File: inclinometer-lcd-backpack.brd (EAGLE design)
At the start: 78.7 x 25.4 mm, 15 parts, among them IC1 ATmega328-DIP-Prgrammed, Q1 2N3904, U1 LCD-16X2NOHOLES, Y1 16MHz

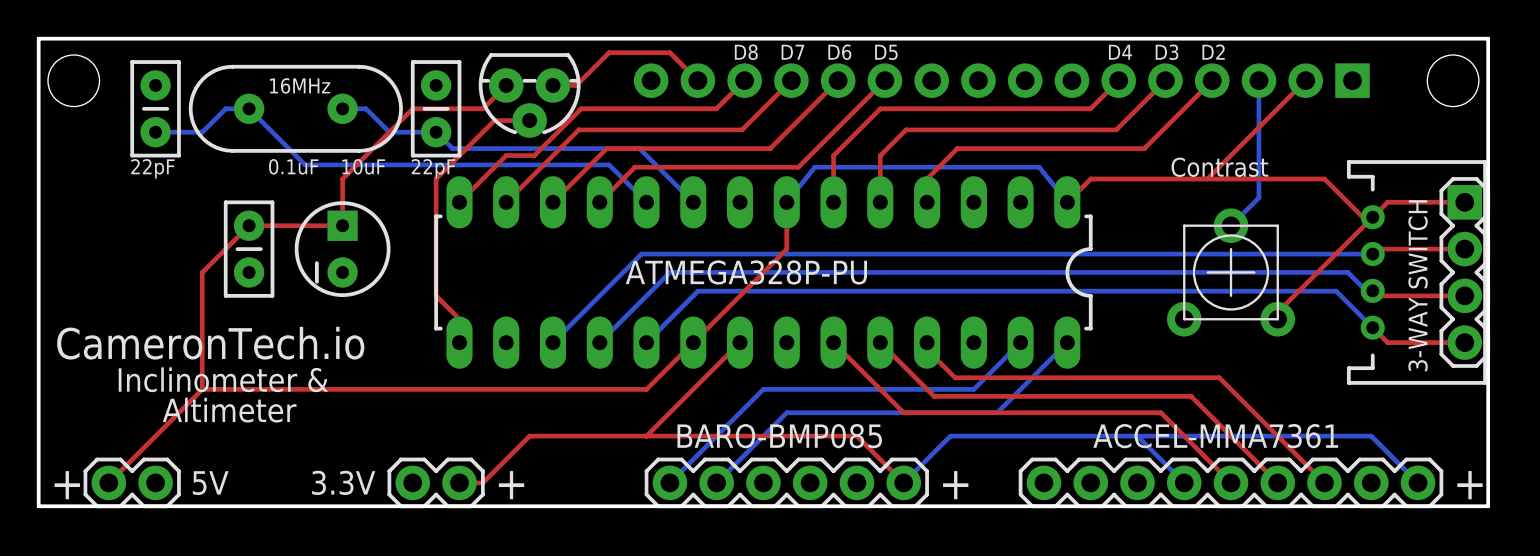
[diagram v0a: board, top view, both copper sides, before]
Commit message: Moved pins away from bottom edge, updated silkscreen
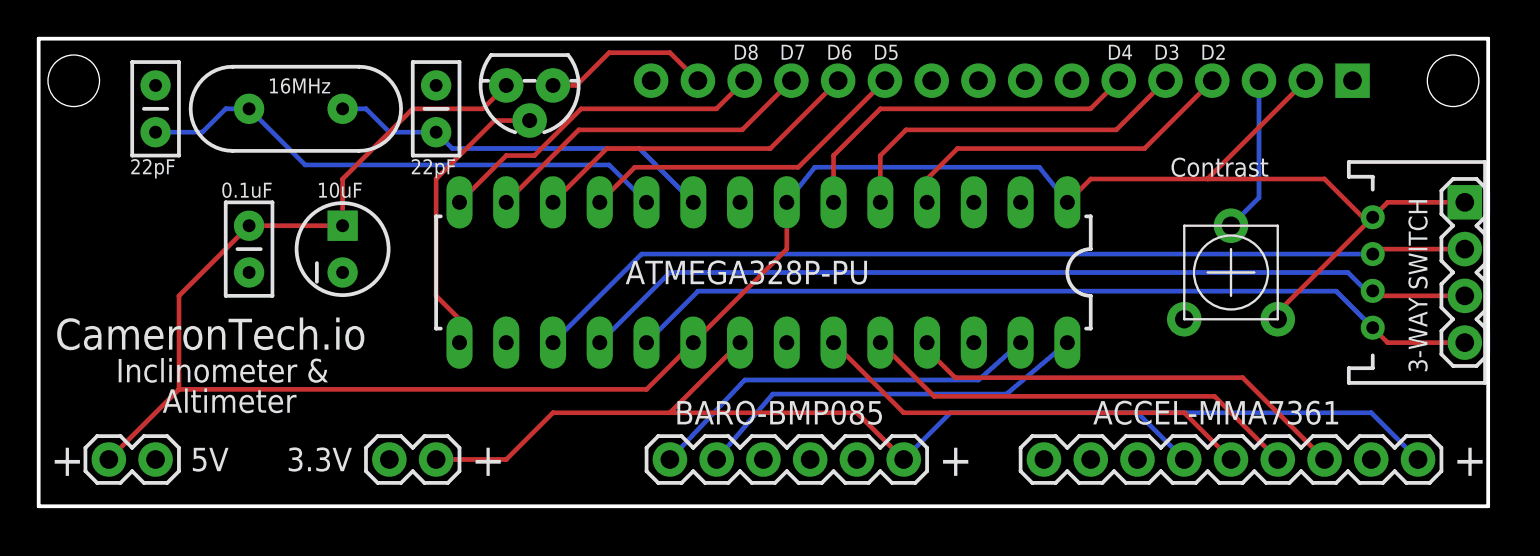
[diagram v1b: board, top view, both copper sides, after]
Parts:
- moved 3.3V 1.80 mm to (19.1, 2.54)
- moved 5V 1.27 mm to (6.35, 2.54)
- moved ACCEL 1.27 mm to (54.6, 2.54)
- moved BARO 1.27 mm to (47.0, 2.54)
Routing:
- net A2: track 25.0 -> 24.4 mm
- net A1: track 24.7 -> 24.2 mm
- net A0: track 24.7 -> 24.2 mm
- net 3.3V: track 67.1 -> 66.5 mm
- net A4: track 22.2 -> 21.7 mm

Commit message: Changes 3-way switch from 5V to GND, beefs up power connections to 0.016 wire width
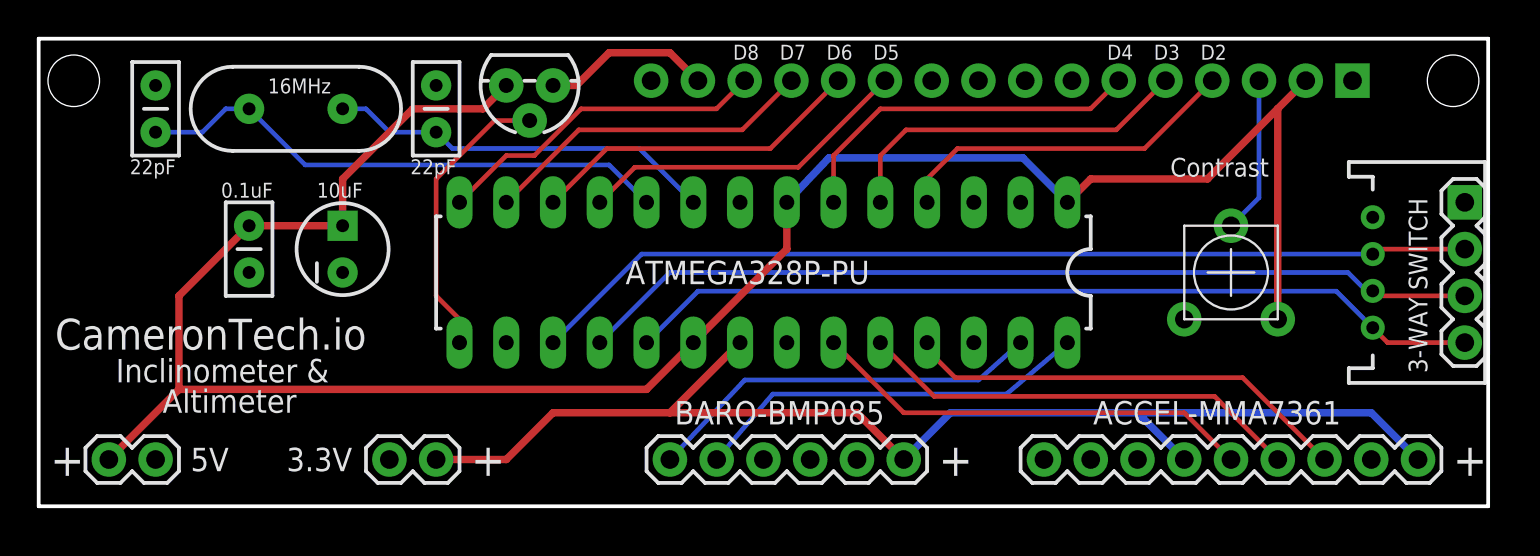
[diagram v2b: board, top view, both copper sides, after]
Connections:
- net 5V: no longer SWITCH-JST.1, SWITCH.1
- net GND: now also SWITCH-JST.1, SWITCH.1
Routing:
- net 5V: track 128.8 -> 117.6 mm
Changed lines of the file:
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@@
 <grid distance="0.05" unitdist="inch" unit="inch" style="lines" multiple="1" display="yes" altdistance="0.005" altunitdist="inch" altunit="inch"/>
 <layers>
-<layer number="1" name="Top" color="4" fill="1" visible="no" active="yes"/>
+<layer number="1" name="Top" color="4" fill="1" visible="yes" active="yes"/>
 <layer number="2" name="Route2" color="1" fill="3" visible="no" active="no"/>
 <layer number="3" name="Route3" color="4" fill="3" visible="no" active="no"/>
@@
 <layer number="14" name="Route14" color="1" fill="6" visible="no" active="no"/>
 <layer number="15" name="Route15" color="4" fill="6" visible="no" active="no"/>
-<layer number="16" name="Bottom" color="1" fill="1" visible="no" active="yes"/>
+<layer number="16" name="Bottom" color="1" fill="1" visible="yes" active="yes"/>
 <layer number="17" name="Pads" color="2" fill="1" visible="yes" active="yes"/>
 <layer number="18" name="Vias" color="2" fill="1" visible="yes" active="yes"/>
@@
 <layer number="21" name="tPlace" color="16" fill="1" visible="no" active="yes"/>
 <layer number="22" name="bPlace" color="14" fill="1" visible="yes" active="yes"/>
-<layer number="23" name="tOrigins" color="15" fill="1" visible="no" active="yes"/>
-<layer number="24" name="bOrigins" color="15" fill="1" visible="no" active="yes"/>
+<layer number="23" name="tOrigins" color="15" fill="1" visible="yes" active="yes"/>
+<layer number="24" name="bOrigins" color="15" fill="1" visible="yes" active="yes"/>
 <layer number="25" name="tNames" color="7" fill="1" visible="no" active="yes"/>
-<layer number="26" name="bNames" color="7" fill="1" visible="yes" active="yes"/>
+<layer number="26" name="bNames" color="7" fill="1" visible="no" active="yes"/>
 <layer number="27" name="tValues" color="7" fill="1" visible="no" active="yes"/>
 <layer number="28" name="bValues" color="7" fill="1" visible="no" active="yes"/>
@@
 <layer number="49" name="Reference" color="7" fill="1" visible="no" active="yes"/>
 <layer number="50" name="dxf" color="7" fill="1" visible="no" active="yes"/>
-<layer number="51" name="tDocu" color="6" fill="1" visible="no" active="yes"/>
+<layer number="51" name="tDocu" color="6" fill="1" visible="yes" active="yes"/>
 <layer number="52" name="bDocu" color="7" fill="1" visible="no" active="yes"/>
 <layer number="53" name="tGND_GNDA" color="7" fill="9" visible="no" active="no"/>
@@
 <contactref element="U1" pad="2"/>
 <contactref element="Q1" pad="3"/>
-<wire x1="24.13" y1="21.59" x2="25.4" y2="22.86" width="0.254" layer="1"/>
-<wire x1="20.32" y1="21.59" x2="24.13" y2="21.59" width="0.254" layer="1"/>
-<wire x1="11.43" y1="15.24" x2="16.51" y2="15.24" width="0.254" layer="1"/>
-<wire x1="16.51" y1="15.24" x2="16.51" y2="17.78" width="0.254" layer="1"/>
-<wire x1="16.51" y1="17.78" x2="20.32" y2="21.59" width="0.254" layer="1"/>
-<wire x1="33.02" y1="6.35" x2="35.56" y2="8.89" width="0.254" layer="1"/>
-<wire x1="40.64" y1="13.97" x2="40.64" y2="16.51" width="0.254" layer="1"/>
-<wire x1="7.62" y1="11.43" x2="11.43" y2="15.24" width="0.254" layer="1"/>
-<wire x1="7.62" y1="11.43" x2="7.62" y2="6.35" width="0.254" layer="1"/>
+<wire x1="24.13" y1="21.59" x2="25.4" y2="22.86" width="0.4064" layer="1"/>
+<wire x1="20.32" y1="21.59" x2="24.13" y2="21.59" width="0.4064" layer="1"/>
+<wire x1="11.43" y1="15.24" x2="16.51" y2="15.24" width="0.4064" layer="1"/>
+<wire x1="16.51" y1="15.24" x2="16.51" y2="17.78" width="0.4064" layer="1"/>
+<wire x1="16.51" y1="17.78" x2="20.32" y2="21.59" width="0.4064" layer="1"/>
+<wire x1="33.02" y1="6.35" x2="35.56" y2="8.89" width="0.4064" layer="1"/>
+<wire x1="40.64" y1="13.97" x2="40.64" y2="16.51" width="0.4064" layer="1"/>
+<wire x1="7.62" y1="11.43" x2="11.43" y2="15.24" width="0.4064" layer="1"/>
+<wire x1="7.62" y1="11.43" x2="7.62" y2="6.35" width="0.4064" layer="1"/>
 <contactref element="5V" pad="2"/>
-<wire x1="3.81" y1="2.54" x2="7.62" y2="6.35" width="0.254" layer="1"/>
-<wire x1="33.02" y1="6.35" x2="7.62" y2="6.35" width="0.254" layer="1"/>
-<wire x1="35.56" y1="8.89" x2="40.64" y2="13.97" width="0.254" layer="1"/>
+<wire x1="3.81" y1="2.54" x2="7.62" y2="6.35" width="0.4064" layer="1"/>
+<wire x1="33.02" y1="6.35" x2="7.62" y2="6.35" width="0.4064" layer="1"/>
+<wire x1="35.56" y1="8.89" x2="40.64" y2="13.97" width="0.4064" layer="1"/>
 <contactref element="R2" pad="3"/>
-<contactref element="SWITCH-JST" pad="1"/>
 <contactref element="IC1" pad="1"/>
-<wire x1="55.88" y1="16.51" x2="57.15" y2="17.78" width="0.254" layer="1"/>
-<wire x1="57.15" y1="17.78" x2="63.5" y2="17.78" width="0.254" layer="1"/>
-<wire x1="63.5" y1="17.78" x2="69.85" y2="17.78" width="0.254" layer="1"/>
-<wire x1="69.85" y1="17.78" x2="71.93" y2="15.7" width="0.254" layer="1"/>
-<wire x1="71.93" y1="15.7" x2="72.47" y2="15.7" width="0.254" layer="1"/>
-<wire x1="68.83" y1="23.12" x2="63.5" y2="17.79" width="0.254" layer="1"/>
+<wire x1="55.88" y1="16.51" x2="57.15" y2="17.78" width="0.4064" layer="1"/>
+<wire x1="57.15" y1="17.78" x2="63.5" y2="17.78" width="0.4064" layer="1"/>
+<wire x1="68.83" y1="23.12" x2="67.305" y2="21.595" width="0.4064" layer="1"/>
+<wire x1="67.305" y1="21.595" x2="63.5" y2="17.79" width="0.4064" layer="1"/>
 <wire x1="63.5" y1="17.79" x2="63.5" y2="17.78" width="0.254" layer="1"/>
-<wire x1="55.88" y1="16.51" x2="54.356" y2="18.415" width="0.254" layer="16"/>
-<wire x1="54.356" y1="18.415" x2="42.164" y2="18.415" width="0.254" layer="16"/>
-<wire x1="42.164" y1="18.415" x2="40.64" y2="16.51" width="0.254" layer="16"/>
-<contactref element="SWITCH" pad="1"/>
-<wire x1="77.47" y1="16.51" x2="73.28" y2="16.51" width="0.254" layer="1"/>
-<wire x1="73.28" y1="16.51" x2="72.47" y2="15.7" width="0.254" layer="1"/>
-<wire x1="67.31" y1="10.16" x2="67.31" y2="10.54" width="0.254" layer="1"/>
-<wire x1="67.31" y1="10.54" x2="72.47" y2="15.7" width="0.254" layer="1"/>
+<wire x1="55.88" y1="16.51" x2="53.467" y2="18.923" width="0.4064" layer="16"/>
+<wire x1="53.467" y1="18.923" x2="42.926" y2="18.923" width="0.4064" layer="16"/>
+<wire x1="42.926" y1="18.923" x2="40.64" y2="16.51" width="0.4064" layer="16"/>
+<wire x1="67.31" y1="10.16" x2="67.31" y2="21.59" width="0.4064" layer="1"/>
+<wire x1="67.31" y1="21.59" x2="67.305" y2="21.595" width="0.254" layer="1"/>
 </signal>
 <signal name="GND">
@@
 <contactref element="ACCEL" pad="8"/>
 <contactref element="R2" pad="1"/>
+<contactref element="SWITCH-JST" pad="1"/>
+<contactref element="SWITCH" pad="1"/>
 </signal>
 <signal name="D13">
@@
 <contactref element="U1" pad="15"/>
 <contactref element="Q1" pad="1"/>
-<wire x1="27.94" y1="22.86" x2="29.21" y2="22.86" width="0.254" layer="1"/>
-<wire x1="34.292" y1="24.638" x2="35.81" y2="23.12" width="0.254" layer="1"/>
-<wire x1="29.21" y1="22.86" x2="30.988" y2="24.638" width="0.254" layer="1"/>
-<wire x1="30.988" y1="24.638" x2="34.292" y2="24.638" width="0.254" layer="1"/>
+<wire x1="27.94" y1="22.86" x2="29.21" y2="22.86" width="0.4064" layer="1"/>
+<wire x1="34.292" y1="24.638" x2="35.81" y2="23.12" width="0.4064" layer="1"/>
+<wire x1="29.21" y1="22.86" x2="30.988" y2="24.638" width="0.4064" layer="1"/>
+<wire x1="30.988" y1="24.638" x2="34.292" y2="24.638" width="0.4064" layer="1"/>
 </signal>
 <signal name="D11">
@@
 <contactref element="ACCEL" pad="4"/>
 <contactref element="ACCEL" pad="9"/>
-<wire x1="21.59" y1="2.54" x2="25.4" y2="2.54" width="0.254" layer="1"/>
-<wire x1="25.4" y1="2.54" x2="27.94" y2="5.08" width="0.254" layer="1"/>
-<wire x1="27.94" y1="5.08" x2="34.29" y2="5.08" width="0.254" layer="1"/>
-<wire x1="34.29" y1="5.08" x2="38.1" y2="8.89" width="0.254" layer="1"/>
-<wire x1="46.99" y1="2.54" x2="44.45" y2="5.08" width="0.254" layer="1"/>
-<wire x1="44.45" y1="5.08" x2="34.29" y2="5.08" width="0.254" layer="1"/>
-<wire x1="46.99" y1="2.54" x2="49.53" y2="5.08" width="0.254" layer="16"/>
-<wire x1="49.53" y1="5.08" x2="59.69" y2="5.08" width="0.254" layer="16"/>
-<wire x1="59.69" y1="5.08" x2="62.23" y2="2.54" width="0.254" layer="16"/>
-<wire x1="74.93" y1="2.54" x2="72.39" y2="5.08" width="0.254" layer="16"/>
-<wire x1="72.39" y1="5.08" x2="59.69" y2="5.08" width="0.254" layer="16"/>
+<wire x1="21.59" y1="2.54" x2="25.4" y2="2.54" width="0.4064" layer="1"/>
+<wire x1="25.4" y1="2.54" x2="27.94" y2="5.08" width="0.4064" layer="1"/>
+<wire x1="27.94" y1="5.08" x2="34.29" y2="5.08" width="0.4064" layer="1"/>
+<wire x1="34.29" y1="5.08" x2="38.1" y2="8.89" width="0.4064" layer="1"/>
+<wire x1="46.99" y1="2.54" x2="44.45" y2="5.08" width="0.4064" layer="1"/>
+<wire x1="44.45" y1="5.08" x2="34.29" y2="5.08" width="0.4064" layer="1"/>
+<wire x1="46.99" y1="2.54" x2="49.53" y2="5.08" width="0.4064" layer="16"/>
+<wire x1="49.53" y1="5.08" x2="59.69" y2="5.08" width="0.4064" layer="16"/>
+<wire x1="59.69" y1="5.08" x2="62.23" y2="2.54" width="0.4064" layer="16"/>
+<wire x1="74.93" y1="2.54" x2="72.39" y2="5.08" width="0.4064" layer="16"/>
+<wire x1="72.39" y1="5.08" x2="59.69" y2="5.08" width="0.4064" layer="16"/>
 </signal>
 </signals>

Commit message: Removes extra voltage smoothing caps (dual regulator board is doing this already)
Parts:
- removed C3: 10uF, SparkFun:CPOL-RADIAL-10UF-25V
- removed C4: 0.1uF, SparkFun:CAP-PTH-SMALL2
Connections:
- net 5V: no longer C3.1, C4.1
- net GND: no longer C3.2, C4.2
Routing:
- net 5V: track 117.6 -> 114.6 mm
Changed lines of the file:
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@@
 <layer number="19" name="Unrouted" color="6" fill="1" visible="yes" active="yes"/>
 <layer number="20" name="Dimension" color="15" fill="1" visible="yes" active="yes"/>
-<layer number="21" name="tPlace" color="16" fill="1" visible="no" active="yes"/>
+<layer number="21" name="tPlace" color="16" fill="1" visible="yes" active="yes"/>
 <layer number="22" name="bPlace" color="14" fill="1" visible="yes" active="yes"/>
 <layer number="23" name="tOrigins" color="15" fill="1" visible="yes" active="yes"/>
 <layer number="24" name="bOrigins" color="15" fill="1" visible="yes" active="yes"/>
-<layer number="25" name="tNames" color="7" fill="1" visible="no" active="yes"/>
+<layer number="25" name="tNames" color="7" fill="1" visible="yes" active="yes"/>
 <layer number="26" name="bNames" color="7" fill="1" visible="no" active="yes"/>
 <layer number="27" name="tValues" color="7" fill="1" visible="no" active="yes"/>
@@
 <attribute name="VALUE" x="24.13" y="19.05" size="0.6096" layer="27" rot="R90"/>
 </element>
-<element name="C3" library="SparkFun" package="CPOL-RADIAL-10UF-25V" value="10uF" x="16.51" y="13.97" smashed="yes" rot="R90">
-<attribute name="VALUE" x="20.193" y="12.065" size="0.8128" layer="27" rot="R90"/>
-</element>
-<element name="C4" library="SparkFun" package="CAP-PTH-SMALL2" value="0.1uF" x="11.43" y="15.24" smashed="yes" rot="R270">
-<attribute name="VALUE" x="8.89" y="16.51" size="0.6096" layer="27" rot="R270"/>
-</element>
 <element name="U1" library="SparkFun-Displays" package="LCD-16X2_NOHOLES" value="LCD-16X2NOHOLES" x="39.37" y="7.62" rot="MR0"/>
 <element name="Q1" library="SparkFun" package="TO-92" value="2N3904" x="26.67" y="22.86" smashed="yes" rot="R180">
@@
 <contactref element="IC1" pad="7"/>
 <contactref element="IC1" pad="20"/>
-<contactref element="C3" pad="1"/>
-<contactref element="C4" pad="1"/>
 <contactref element="U1" pad="2"/>
 <contactref element="Q1" pad="3"/>
 <wire x1="24.13" y1="21.59" x2="25.4" y2="22.86" width="0.4064" layer="1"/>
 <wire x1="20.32" y1="21.59" x2="24.13" y2="21.59" width="0.4064" layer="1"/>
-<wire x1="11.43" y1="15.24" x2="16.51" y2="15.24" width="0.4064" layer="1"/>
-<wire x1="16.51" y1="15.24" x2="16.51" y2="17.78" width="0.4064" layer="1"/>
-<wire x1="16.51" y1="17.78" x2="20.32" y2="21.59" width="0.4064" layer="1"/>
 <wire x1="33.02" y1="6.35" x2="35.56" y2="8.89" width="0.4064" layer="1"/>
 <wire x1="40.64" y1="13.97" x2="40.64" y2="16.51" width="0.4064" layer="1"/>
-<wire x1="7.62" y1="11.43" x2="11.43" y2="15.24" width="0.4064" layer="1"/>
-<wire x1="7.62" y1="11.43" x2="7.62" y2="6.35" width="0.4064" layer="1"/>
 <contactref element="5V" pad="2"/>
 <wire x1="3.81" y1="2.54" x2="7.62" y2="6.35" width="0.4064" layer="1"/>
@@
 <wire x1="67.31" y1="10.16" x2="67.31" y2="21.59" width="0.4064" layer="1"/>
 <wire x1="67.31" y1="21.59" x2="67.305" y2="21.595" width="0.254" layer="1"/>
+<wire x1="7.62" y1="6.35" x2="7.62" y2="8.89" width="0.4064" layer="1"/>
+<wire x1="7.62" y1="8.89" x2="20.32" y2="21.59" width="0.4064" layer="1"/>
 </signal>
 <signal name="GND">
@@
 <contactref element="C2" pad="2"/>
 <contactref element="C1" pad="2"/>
-<contactref element="C3" pad="2"/>
-<contactref element="C4" pad="2"/>
 <contactref element="U1" pad="1"/>
 <contactref element="U1" pad="16"/>
